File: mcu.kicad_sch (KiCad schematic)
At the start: 40 parts, among them J2 Conn_01x05, J3 Conn_01x10, J4 Conn_01x10, Q1 BC817, Q2 BC817, SW1 SW_Push, SW2 SW_Push, SW3 SW_Push, U4 ESP32-S3-WROOM-1, U5 CP2102N-A02-GQFN28R

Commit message: Make lcsc field compatible with plugin
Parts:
- C15, C20, C26: LCSC PN (none) -> C96446; LCSC Part C96446 -> (none)
- C16, C18, C19, C22, C23, C24, C25: LCSC PN (none) -> C14663; LCSC Part C14663 -> (none)
- C17, C21: LCSC PN (none) -> C29936; LCSC Part C29936 -> (none)
- D3, D4, D5, D6: LCSC PN (none) -> C965555; LCSC Part C965555 -> (none)
- J2: LCSC PN (none) -> C5116488; LCSC Part C5116488 -> (none)
- J3, J4: LCSC PN (none) -> C5116489; LCSC Part C5116489 -> (none)
- Q1, Q2: LCSC PN (none) -> C39828; LCSC Part C39828 -> (none)
- R10, R11, R12, R13, R6, R9: LCSC PN (none) -> C98220; LCSC Part C98220 -> (none)
- R3: LCSC PN (none) -> C137768; LCSC Part C137768 -> (none)
- R4: LCSC PN (none) -> C22548; LCSC Part C22548 -> (none)
- R5: LCSC PN (none) -> C137715; LCSC Part C137715 -> (none)
- R7, R8: LCSC PN (none) -> C99782; LCSC Part C99782 -> (none)
- SW1, SW2, SW3: LCSC PN (none) -> C720477; LCSC Part C720477 -> (none)
- U4: LCSC PN (none) -> C2913202; LCSC Part C2913202 -> (none)
- U5: LCSC PN (none) -> C964632; LCSC Part C964632 -> (none)
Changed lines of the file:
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@@
 			)
 		)
-		(property "LCSC Part" "C96446"
+		(property "LCSC PN" "C96446"
 			(at 265.43 138.43 0)
 			(effects
@@
 			)
 		)
-		(property "LCSC Part" "C965555"
+		(property "LCSC PN" "C965555"
 			(at 167.64 118.11 0)
 			(effects
@@
 			)
 		)
-		(property "LCSC Part" "C99782"
+		(property "LCSC PN" "C99782"
 			(at 44.45 87.63 0)
 			(effects
@@
 			)
 		)
-		(property "LCSC Part" "C98220"
+		(property "LCSC PN" "C98220"
 			(at 106.68 124.46 0)
 			(effects
@@
 			)
 		)
-		(property "LCSC Part" "C2913202"
+		(property "LCSC PN" "C2913202"
 			(at 106.68 69.85 0)
 			(effects
@@
 			)
 		)
-		(property "LCSC Part" "C39828"
+		(property "LCSC PN" "C39828"
 			(at 240.03 100.33 0)
 			(effects
@@
 			)
 		)
-		(property "LCSC Part" "C14663"
+		(property "LCSC PN" "C14663"
 			(at 250.19 48.26 0)
 			(effects
@@
 			)
 		)
-		(property "LCSC Part" "C98220"
+		(property "LCSC PN" "C98220"
 			(at 139.7 113.03 0)
 			(effects
@@
 			)
 		)
-		(property "LCSC Part" "C137715"
+		(property "LCSC PN" "C137715"
 			(at 170.18 54.61 0)
 			(effects
@@
 			)
 		)
-		(property "LCSC Part" "C14663"
+		(property "LCSC PN" "C14663"
 			(at 240.03 138.43 0)
 			(effects
@@
 			)
 		)
-		(property "LCSC Part" "C14663"
+		(property "LCSC PN" "C14663"
 			(at 214.63 138.43 0)
 			(effects
@@
 			)
 		)
-		(property "LCSC Part" "C720477"
+		(property "LCSC PN" "C720477"
 			(at 71.12 135.89 90)
 			(effects
@@
 			)
 		)
-		(property "LCSC Part" "C720477"
+		(property "LCSC PN" "C720477"
 			(at 106.68 135.89 90)
 			(effects
@@
 			)
 		)
-		(property "LCSC Part" "C5116489"
+		(property "LCSC PN" "C5116489"
 			(at 113.03 170.18 0)
 			(effects
@@
 			)
 		)
-		(property "LCSC Part" "C98220"
+		(property "LCSC PN" "C98220"
 			(at 43.18 124.46 0)
 			(effects
@@
 			)
 		)
-		(property "LCSC Part" "C39828"
+		(property "LCSC PN" "C39828"
 			(at 240.03 85.09 0)
 			(effects
@@
 			)
 		)
-		(property "LCSC Part" "C5116488"
+		(property "LCSC PN" "C5116488"
 			(at 72.39 165.1 0)
 			(effects
@@
 			)
 		)
-		(property "LCSC Part" "C965555"
+		(property "LCSC PN" "C965555"
 			(at 152.4 118.11 0)
 			(effects
@@
 			)
 		)
-		(property "LCSC Part" "C29936"
+		(property "LCSC PN" "C29936"
 			(at 156.21 48.26 0)
 			(effects
@@
 			)
 		)
-		(property "LCSC Part" "C14663"
+		(property "LCSC PN" "C14663"
 			(at 252.73 138.43 0)
 			(effects
@@
 			)
 		)
-		(property "LCSC Part" "C5116489"
+		(property "LCSC PN" "C5116489"
 			(at 152.4 170.18 0)
 			(effects
@@
 			)
 		)
-		(property "LCSC Part" "C137768"
+		(property "LCSC PN" "C137768"
 			(at 170.18 44.45 0)
 			(effects
@@
 			)
 		)
-		(property "LCSC Part" "C29936"
+		(property "LCSC PN" "C29936"
 			(at 83.82 135.89 0)
 			(effects
@@
 			)
 		)
-		(property "LCSC Part" "C965555"
+		(property "LCSC PN" "C965555"
 			(at 198.12 118.11 0)
 			(effects
@@
 			)
 		)
-		(property "LCSC Part" "C96446"
+		(property "LCSC PN" "C96446"
 			(at 264.16 48.26 0)
 			(effects
@@
 			)
 		)
-		(property "LCSC Part" "C22548"
+		(property "LCSC PN" "C22548"
 			(at 208.28 44.45 0)
 			(effects
@@
 			)
 		)
-		(property "LCSC Part" "C98220"
+		(property "LCSC PN" "C98220"
 			(at 248.92 100.33 90)
 			(effects
@@
 			)
 		)
-		(property "LCSC Part" "C965555"
+		(property "LCSC PN" "C965555"
 			(at 182.88 118.11 0)
 			(effects
@@
 			)
 		)
-		(property "LCSC Part" "C98220"
+		(property "LCSC PN" "C98220"
 			(at 71.12 124.46 0)
 			(effects
@@
 			)
 		)
-		(property "LCSC Part" "C720477"
+		(property "LCSC PN" "C720477"
 			(at 43.18 135.89 90)
 			(effects
@@
 			)
 		)
-		(property "LCSC Part" "C14663"
+		(property "LCSC PN" "C14663"
 			(at 53.34 48.26 0)
 			(effects
@@
 			)
 		)
-		(property "LCSC Part" "C98220"
+		(property "LCSC PN" "C98220"
 			(at 248.92 85.09 90)
 			(effects
@@
 			)
 		)
-		(property "LCSC Part" "C14663"
+		(property "LCSC PN" "C14663"
 			(at 236.22 48.26 0)
 			(effects
@@
 			)
 		)
-		(property "LCSC Part" "C96446"
+		(property "LCSC PN" "C96446"
 			(at 40.64 48.26 0)
 			(effects
@@
 			)
 		)
-		(property "LCSC Part" "C99782"
+		(property "LCSC PN" "C99782"
 			(at 53.34 87.63 0)
 			(effects
@@
 			)
 		)
-		(property "LCSC Part" "C14663"
+		(property "LCSC PN" "C14663"
 			(at 227.33 138.43 0)
 			(effects
@@
 			)
 		)
-		(property "LCSC Part" "C964632"
+		(property "LCSC PN" "C964632"
 			(at 187.96 69.85 0)
 			(effects

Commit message: Exclude test points from BOM
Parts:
- TP5, TP6, TP7: now left out of the parts list
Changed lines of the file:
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@@
 		(unit 1)
 		(exclude_from_sim no)
-		(in_bom yes)
+		(in_bom no)
 		(on_board yes)
 		(dnp no)
@@
 		(unit 1)
 		(exclude_from_sim no)
-		(in_bom yes)
+		(in_bom no)
 		(on_board yes)
 		(dnp no)
@@
 		(unit 1)
 		(exclude_from_sim no)
-		(in_bom yes)
+		(in_bom no)
 		(on_board yes)
 		(dnp no)

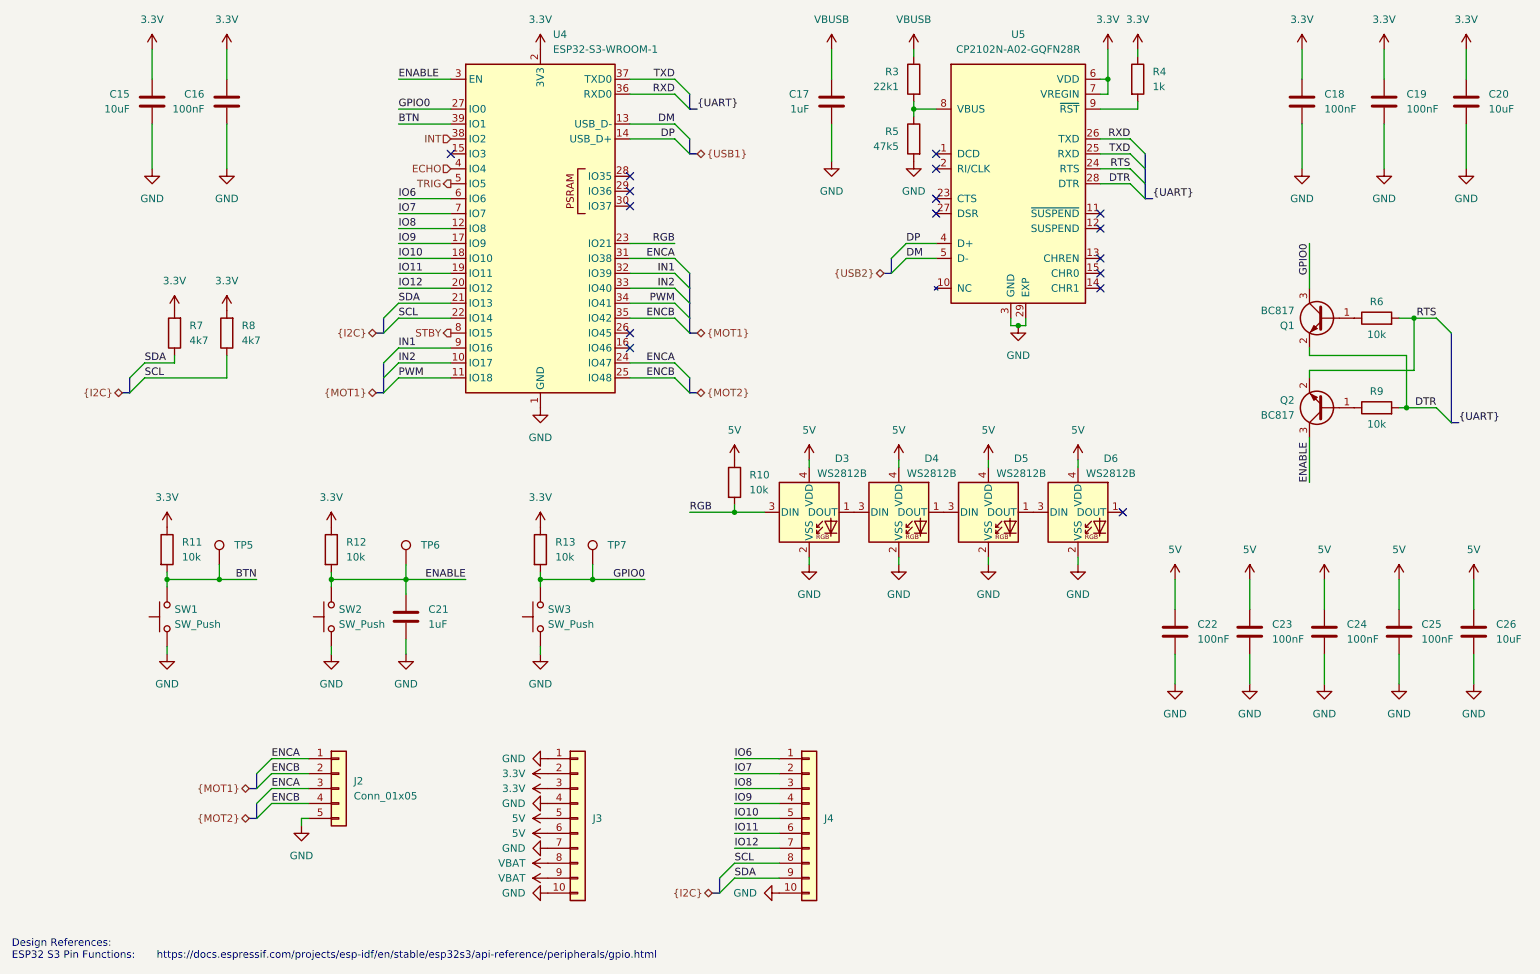
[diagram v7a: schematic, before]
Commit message: Add missing rgb leds
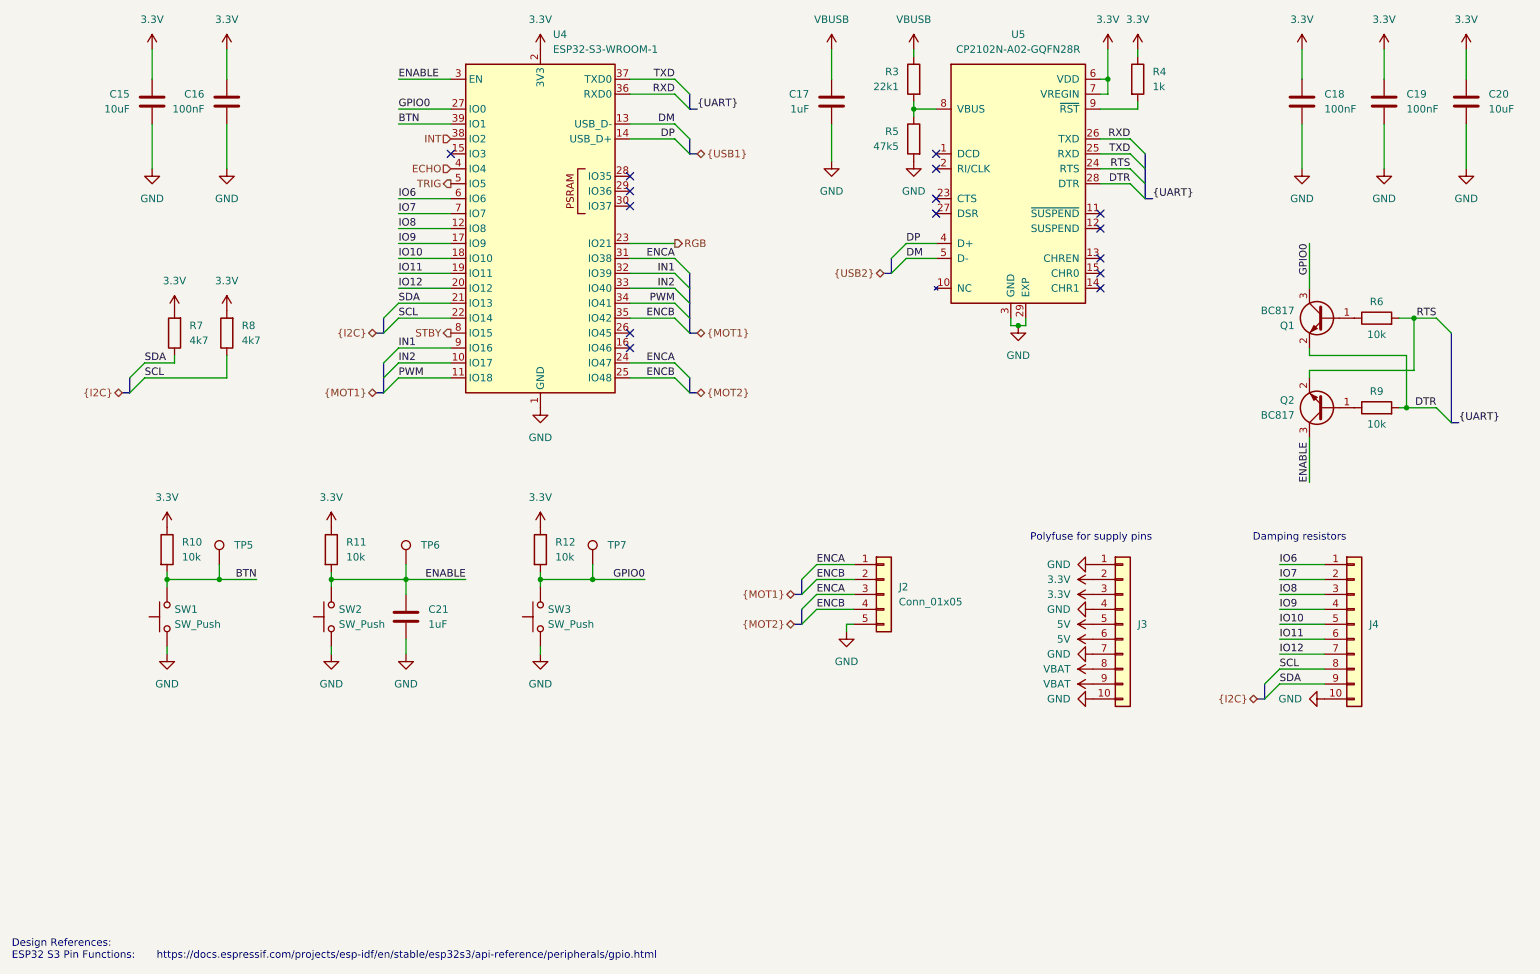
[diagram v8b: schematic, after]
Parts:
- removed C22, C23, C24, C25: 100nF, Capacitor_SMD:C_0603_1608Metric_Pad1.08x0.95mm_HandSolder, symbol Device:C
- removed C26: 10uF, Capacitor_SMD:C_0603_1608Metric_Pad1.08x0.95mm_HandSolder, symbol Device:C
- removed D3, D4, D5, D6: WS2812B, LED_SMD:LED_WS2812B-2020_PLCC4_2.0x2.0mm, symbol LED:WS2812B-2020
- removed R10: 10k, Resistor_SMD:R_0603_1608Metric_Pad0.98x0.95mm_HandSolder, symbol Device:R
- renumbered R11 to R10, R12 to R11, R13 to R12
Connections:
- no-connect marks 16 -> 15
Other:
- note added: "Damping resistors"
- note added: "Polyfuse for supply pins"
- moved on the sheet: J2, J3, J4
